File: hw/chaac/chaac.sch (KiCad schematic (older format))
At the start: 94 parts, among them J1 windrain, J10 Solar Panel, J2 RP_SMA, J3 UART, J4 Battery, J5 Power, J6 Light, J7 AM2315, J8 TC2030-CTX, J9 Therm, Q1 Q_PMOS_GSD, SW1 RST, SW2 RST, U1 MIC550X, U2 NRF52811-QFAA, U3 XBEE_S2C, U5 BMP280, U6 MCP73871, Y1 32.768kHz, Y2 32MHz

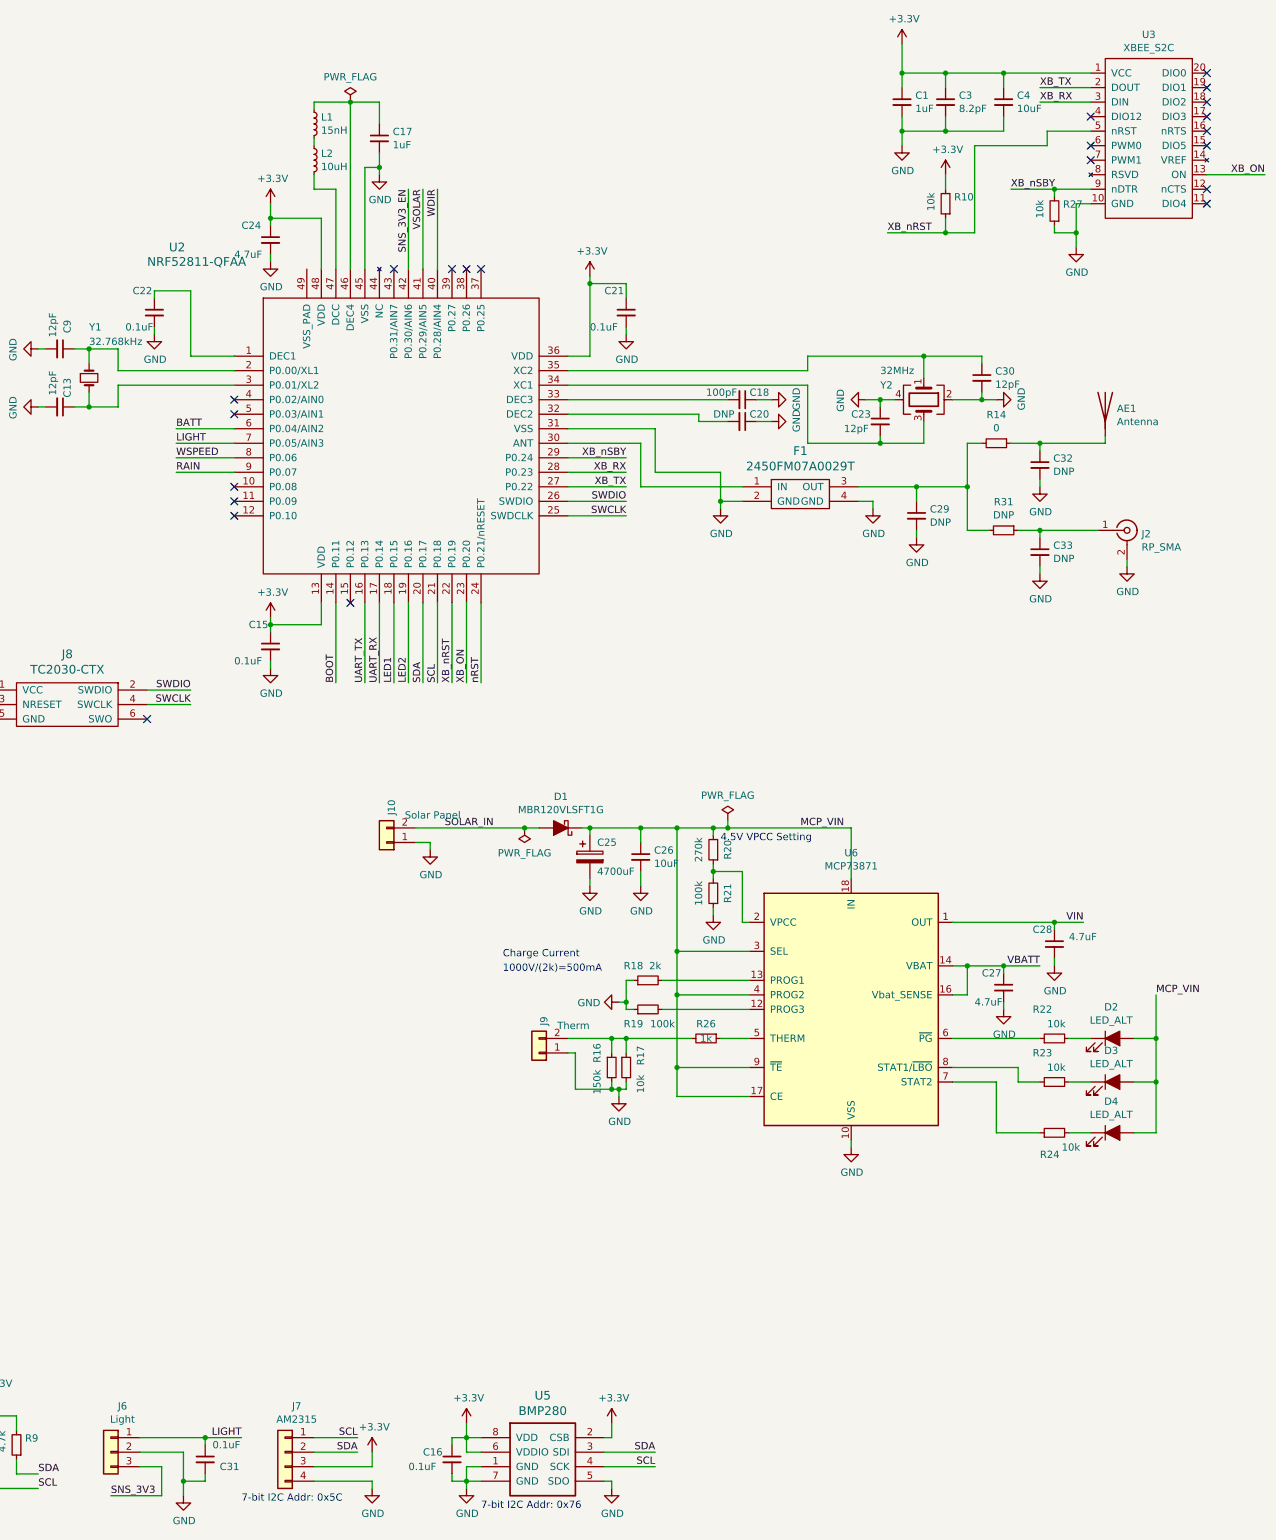
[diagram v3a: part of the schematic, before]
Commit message: Released chaac v2.0 to JLCPCB
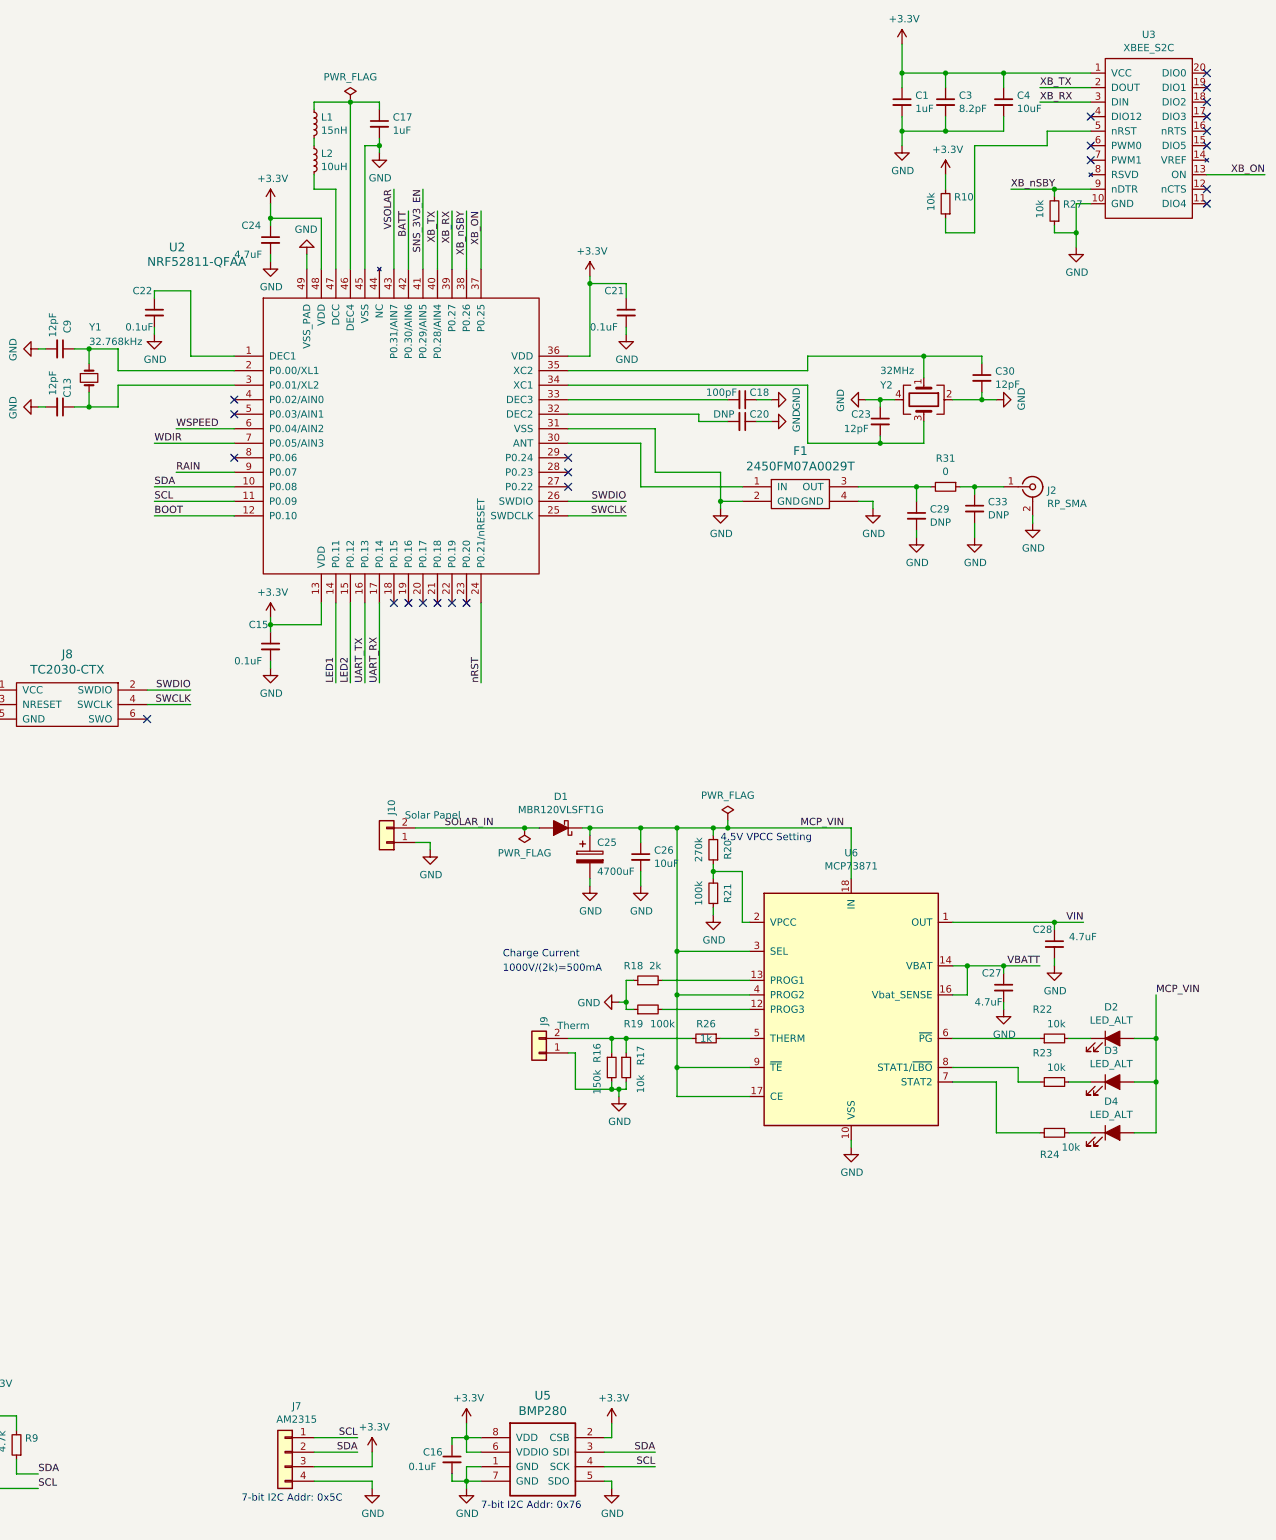
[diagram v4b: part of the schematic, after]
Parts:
- removed AE1: Antenna, alvarop:AMCA31-2R450G-S1F-T3, symbol Device:Antenna
- removed C31: 0.1uF, Capacitor_SMD:C_0603_1608Metric, symbol Device:C_Small
- removed C32: DNP, Capacitor_SMD:C_0402_1005Metric, symbol Device:C_Small
- removed J6: Light, Connector_PinHeader_2.54mm:PinHeader_1x03_P2.54mm_Vertical, symbol Connector_Generic:Conn_01x03
- removed R14: 0, Resistor_SMD:R_0402_1005Metric, symbol Device:R_Small
- C13, C23, C30, C9: DKPN (none) -> 399-1013-1-ND; MPN (none) -> C0402C120J5GACTU
- C15, C21, C22: DKPN (none) -> 490-1318-1-ND; MPN (none) -> GRM155R61A104KA01D
- C17: DKPN (none) -> 311-1438-1-ND; MPN (none) -> CC0402KRX5R5BB105
- C18: DKPN (none) -> 587-1211-1-ND; MPN (none) -> UMK105CG101JV-F
- C20: footprint Capacitor_SMD:C_0603_1608Metric -> Capacitor_SMD:C_0402_1005Metric; DKPN 490-1532-1-ND -> (none); MPN GRM188R71C104KA01D -> (none)
- F1: DKPN (none) -> 712-1623-1-ND; MPN (none) -> 2450FM07A0029T
- J2: DKPN (none) -> SAM8857-ND‎; MPN (none) -> ‎SMA-J-P-H-ST-EM1‎
- L1: DKPN (none) -> 587-1521-1-ND‎; MPN (none) -> HK100515NJ-T‎
- L2: DKPN (none) -> 490-4025-1-ND‎; MPN (none) -> ‎LQM18FN100M00D‎
- R31: value DNP -> 0; DKPN (none) -> 1276-3480-1-ND; MPN (none) -> RC1005J000CS
- U2: footprint alvarop:LQFP48 -> Package_DFN_QFN:QFN-48-1EP_6x6mm_P0.4mm_EP4.6x4.6mm; DKPN (none) -> ‎1490-1075-1-ND‎; MPN (none) -> ‎NRF52811-QFAA-R‎
- Y1: DKPN (none) -> ‎SER4084CT-ND‎; MPN (none) -> FC-135 32.7680KA-AC0
- Y2: DKPN (none) -> 1253-1118-1-ND; MPN (none) -> CX2016DB32000D0FLJCC
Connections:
- net LIGHT is gone; now on net WDIR: U2.7 (P0.05/AIN3)
- net BATT: now also U2.42 (P0.30/AIN6); no longer U2.6 (P0.04/AIN2)
- net BOOT: now also U2.12 (P0.10); no longer U2.14 (P0.11)
- net GND: now also U2.49 (VSS_PAD)
- net LED1: now also U2.14 (P0.11); no longer U2.18 (P0.15)
- net LED2: now also U2.15 (P0.12); no longer U2.19 (P0.16)
- net SCL: now also U2.11 (P0.09); no longer U2.21 (P0.18)
- net SDA: now also U2.10 (P0.08); no longer U2.20 (P0.17)
- net SNS_3V3_EN: now also U2.41 (P0.29/AIN5); no longer U2.42 (P0.30/AIN6)
- net VSOLAR: now also U2.43 (P0.31/AIN7); no longer U2.41 (P0.29/AIN5)
- net WDIR: no longer U2.40 (P0.28/AIN4)
- net WSPEED: now also U2.6 (P0.04/AIN2); no longer U2.8 (P0.06)
- net XB_ON: now also U2.37 (P0.25); no longer U2.23 (P0.20)
- net XB_RX: now also U2.39 (P0.27); no longer U2.28 (P0.23)
- net XB_TX: now also U2.40 (P0.28/AIN4); no longer U2.27 (P0.22)
- net XB_nSBY: now also U2.38 (P0.26); no longer U2.29 (P0.24)
- net XB_nRST: no longer names the net of R10.1, U3.5 (nRST)
- net XB_nRST: no longer U2.22 (P0.19)
- no-connect marks 29 -> 31
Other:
- moved on the sheet: C17, C33, J2, R31

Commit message: Progress with chaac base
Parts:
- removed C1: 1uF, Capacitor_SMD:C_0603_1608Metric, symbol Device:C_Small
- removed C13, C23, C30, C9: 12pF, Capacitor_SMD:C_0402_1005Metric, symbol Device:C_Small
- removed C15, C21, C22: 0.1uF, Capacitor_SMD:C_0402_1005Metric, symbol Device:C_Small
- removed C17: 1uF, Capacitor_SMD:C_0402_1005Metric, symbol Device:C_Small
- removed C18: 100pF, Capacitor_SMD:C_0402_1005Metric, symbol Device:C_Small
- removed C20, C29, C33: DNP, Capacitor_SMD:C_0402_1005Metric, symbol Device:C_Small
- removed C24: 4.7uF, Capacitor_SMD:C_0603_1608Metric, symbol Device:C_Small
- removed C3: 8.2pF, Capacitor_SMD:C_0603_1608Metric, symbol Device:C_Small
- removed C4: 10uF, Capacitor_SMD:C_0603_1608Metric, symbol Device:C_Small
- removed F1: 2450FM07A0029T, alvarop:2450FM07A0029T, symbol alvarop:2450FM07A0029T
- removed J2: RP_SMA, Connector_Coaxial:SMA_Samtec_SMA-J-P-H-ST-EM1_EdgeMount, symbol Connector:Conn_Coaxial
- removed J8: TC2030-CTX, alvarop:TC2030-NL, symbol alvarop:TC2030-CTX
- removed J9: Therm, Connector_PinHeader_2.54mm:PinHeader_1x02_P2.54mm_Vertical, symbol Connector_Generic:Conn_01x02
- removed L1: 15nH, Inductor_SMD:L_0402_1005Metric, symbol Device:L_Small
- removed L2: 10uH, Inductor_SMD:L_0603_1608Metric, symbol Device:L_Small
- removed R10, R27: 10k, Resistor_SMD:R_0603_1608Metric, symbol Device:R_Small
- removed R16: 150k, Resistor_SMD:R_0603_1608Metric, symbol Device:R_Small
- removed R26: 1k, Resistor_SMD:R_0603_1608Metric, symbol Device:R_Small
- removed R31: 0, Resistor_SMD:R_0402_1005Metric, symbol Device:R_Small
- removed U2: NRF52811-QFAA, Package_DFN_QFN:QFN-48-1EP_6x6mm_P0.4mm_EP4.6x4.6mm, symbol alvarop:NRF52811-QFAA
- removed U3: XBEE_S2C, alvarop:XBEE_S2C_TH, symbol alvarop:XBEE_S2C
- removed Y1: 32.768kHz, Crystal:Crystal_SMD_3215-2Pin_3.2x1.5mm, symbol Device:Crystal_Small
- removed Y2: 32MHz, Crystal:Crystal_SMD_2016-4Pin_2.0x1.6mm, symbol Device:Crystal_GND24
- added U2: CHAAC_RADIO, alvarop:CHAAC_RADIO, symbol alvarop:CHAAC_RADIO
- C25: value 4700uF -> 470uF; footprint alvarop:CP_Elec_18x16.5 -> Capacitor_SMD:CP_Elec_8x10; DKPN PCE3461CT-ND -> PCE4178CT-ND; MPN EEV-FK1C472M -> EEE-HA1A471UP
- SW1, SW2: footprint alvarop:PTS645SM43SMTR92 -> alvarop:PTS820J25MSMTRLFS; DKPN CKN9112CT-ND -> CKN10839CT-ND; MPN PTS645SM43SMTR92 LFS -> PTS820J25MSMTRLFS
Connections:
- net labels added: P0.02-AIN0, P0.03-AIN1, P0.04-AIN2, P0.05-AIN3, P0.06, P0.07, P0.08, P0.11, P0.12, P0.13, P0.14, P0.15, P0.16, P0.17, P0.18, P0.19, P0.20, P0.22, P0.23, P0.24, P0.25, P0.26, P0.27, P0.28-AIN4, P0.29-AIN5, P0.30-AIN6, P0.31-AIN7
- net labels removed: SWCLK, SWDIO, XB_ON, XB_RX, XB_TX, XB_nSBY
- wire segments 380 -> 261
- no-connect marks 31 -> 7
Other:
- moved on the sheet: R17

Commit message: Done routing chaac v3.0 base board?
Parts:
- removed C7: DNP, Capacitor_SMD:C_0603_1608Metric, symbol Device:C_Small
- removed J5: Power, Connector_PinHeader_2.54mm:PinHeader_1x03_P2.54mm_Vertical, symbol Connector_Generic:Conn_01x03
- J10: footprint Connector_PinHeader_2.54mm:PinHeader_1x02_P2.54mm_Vertical -> TerminalBlock_TE-Connectivity:TerminalBlock_TE_282834-2_1x02_P2.54mm_Horizontal
- J7: footprint Connector_PinHeader_2.54mm:PinHeader_1x04_P2.54mm_Vertical -> TerminalBlock_TE-Connectivity:TerminalBlock_TE_282834-4_1x04_P2.54mm_Horizontal
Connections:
- net labels removed: P0.02-AIN0, P0.03-AIN1, P0.04-AIN2, P0.05-AIN3, P0.06, P0.07, P0.08, P0.11, P0.12, P0.13, P0.14, P0.15, P0.16, P0.17, P0.18, P0.19, P0.20, P0.22, P0.23, P0.24, P0.25, P0.26, P0.27, P0.28-AIN4, P0.29-AIN5, P0.30-AIN6, P0.31-AIN7
- wire segments 261 -> 243
- no-connect marks 7 -> 23
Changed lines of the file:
@@
 L Connector_Generic:Conn_01x04 J7
 U 1 1 5BAAE247
-P 9050 10450
-F 0 "J7" H 8970 10767 50  0000 C CNN
-F 1 "AM2315" H 8970 10676 50  0000 C CNN
-F 2 "Connector_PinHeader_2.54mm:PinHeader_1x04_P2.54mm_Vertical" H 9050 10450 50  0001 C CNN
-F 3 "~" H 9050 10450 50  0001 C CNN
-F 4 "ED10563-ND" H 0   0   50  0001 C CNN "DKPN"
-F 5 "OSTVN04A150" H 0   0   50  0001 C CNN "MPN"
-	1    9050 10450
-	-1   0    0    -1
+P 9050 10550
+F 0 "J7" H 8970 10867 50  0000 C CNN
+F 1 "AM2315" H 8970 10776 50  0000 C CNN
+F 2 "TerminalBlock_TE-Connectivity:TerminalBlock_TE_282834-4_1x04_P2.54mm_Horizontal" H 9050 10550 50  0001 C CNN
+F 3 "~" H 9050 10550 50  0001 C CNN
+F 4 "ED10563-ND" H 0   100 50  0001 C CNN "DKPN"
+F 5 "OSTVN04A150" H 0   100 50  0001 C CNN "MPN"
+	1    9050 10550
+	-1   0    0    1
 $EndComp
 Wire Wire Line
@@
 Text Label 9550 10350 2    50   ~ 0
 SCL
-$Comp
-L Connector_Generic:Conn_01x03 J5
-U 1 1 5BAB4149
-P 3300 1000
-F 0 "J5" H 3220 1317 50  0000 C CNN
-F 1 "Power" H 3220 1226 50  0000 C CNN
-F 2 "Connector_PinHeader_2.54mm:PinHeader_1x03_P2.54mm_Vertical" H 3300 1000 50  0001 C CNN
-F 3 "~" H 3300 1000 50  0001 C CNN
-	1    3300 1000
-	-1   0    0    -1
-$EndComp
-Wire Wire Line
-	3500 1000 3850 1000
-Wire Wire Line
-	3850 1000 3850 1100
-Wire Wire Line
-	3500 900  3850 900
-Wire Wire Line
-	3850 900  3850 800
-Wire Wire Line
-	3500 1100 3750 1100
-Text Label 3750 1100 2    50   ~ 0
-VIN
-$Comp
-L power:+3.3V #PWR011
-U 1 1 5BAB8AA0
-P 3850 800
-F 0 "#PWR011" H 3850 650 50  0001 C CNN
-F 1 "+3.3V" H 3865 973 50  0000 C CNN
-F 2 "" H 3850 800 50  0001 C CNN
-F 3 "" H 3850 800 50  0001 C CNN
-	1    3850 800
-	1    0    0    -1
-$EndComp
 $Comp
 L power:GND #PWR012
@@
 Text Label 5850 3600 0    50   ~ 0
 nRST
-Wire Wire Line
-	9700 4600 9700 5150
-Wire Wire Line
-	9600 4600 9600 5150
-Text Label 9600 5150 1    50   ~ 0
-UART_TX
-Text Label 9700 5150 1    50   ~ 0
-UART_RX
 $Comp
 L Connector_Generic:Conn_01x03 J3
@@
 BATT
 $Comp
-L power:GND #PWR0133
-U 1 1 5CAFFDD5
-P 3850 1100
-F 0 "#PWR0133" H 3850 850 50  0001 C CNN
-F 1 "GND" H 3855 927 50  0000 C CNN
-F 2 "" H 3850 1100 50  0001 C CNN
-F 3 "" H 3850 1100 50  0001 C CNN
-	1    3850 1100
-	1    0    0    -1
-$EndComp
-$Comp
 L power:GND #PWR0134
 U 1 1 5CAFFF76
@@
 F 0 "J10" V 9716 6062 50  0000 R CNN
 F 1 "Solar Panel" H 9625 6062 50  0000 R CNN
-F 2 "Connector_PinHeader_2.54mm:PinHeader_1x02_P2.54mm_Vertical" H 9750 6250 50  0001 C CNN
+F 2 "TerminalBlock_TE-Connectivity:TerminalBlock_TE_282834-2_1x02_P2.54mm_Horizontal" H 9750 6250 50  0001 C CNN
 F 3 "~" H 9750 6250 50  0001 C CNN
 F 4 "ED10561-ND" H 0   0   50  0001 C CNN "DKPN"
@@
 	2000 4400 2000 4250
 Connection ~ 2000 4250
-$Comp
-L Device:C_Small C7
-U 1 1 5C97805D
-P 2450 4000
-F 0 "C7" H 2250 4050 50  0000 L CNN
-F 1 "DNP" H 2150 3950 50  0000 L CNN
-F 2 "Capacitor_SMD:C_0603_1608Metric" H 2450 4000 50  0001 C CNN
-F 3 "~" H 2450 4000 50  0001 C CNN
-	1    2450 4000
-	1    0    0    -1
-$EndComp
-Wire Wire Line
-	2450 4100 2450 4250
-Wire Wire Line
-	2450 4250 2000 4250
-Wire Wire Line
-	2200 3800 2450 3800
-Wire Wire Line
-	2450 3900 2450 3800
-Connection ~ 2450 3800
 Wire Wire Line
 	2000 4600 2000 4750
 Wire Wire Line
 	2000 4750 1450 4750
-Wire Wire Line
-	2450 3800 2900 3800
 Text Label 1450 4750 0    50   ~ 0
 SNS_3V3_EN
@@
 Wire Wire Line
 	5200 5000 5200 5050
-Text Label 10400 5150 1    50   ~ 0
-nRST
-Wire Wire Line
-	10400 5150 10400 4600
 Wire Wire Line
 	5700 3600 5850 3600
 Connection ~ 5700 3600
-Wire Wire Line
-	9300 4600 9300 4750
 Wire Wire Line
 	2450 3050 2650 3050
@@
 	-1   0    0    1
 $EndComp
-Text Label 9500 5150 1    50   ~ 0
-LED2
-Wire Wire Line
-	9500 4600 9500 5150
-Wire Wire Line
-	9400 4600 9400 5150
-Text Label 9400 5150 1    50   ~ 0
-LED1
-Wire Wire Line
-	11250 2600 11250 2050
-Text Label 11250 2050 3    50   ~ 0
+Wire Wire Line
+	6700 6750 7250 6750
+Text Label 4600 8050 0    50   ~ 0
 SNS_3V3_EN
-Text Label 11150 2200 3    50   ~ 0
-BATT
-Wire Wire Line
-	11150 2600 11150 2200
-Text Label 11050 2050 3    50   ~ 0
-VSOLAR
-Wire Wire Line
-	11050 2600 11050 2050
-Wire Wire Line
-	6700 6750 7250 6750
-Text Label 7250 6750 2    50   ~ 0
-P0.26
 Wire Wire Line
 	6700 6850 7250 6850
-Text Label 7250 6850 2    50   ~ 0
-P0.28-AIN4
 Wire Wire Line
 	6700 6950 7250 6950
-Text Label 7250 6950 2    50   ~ 0
-P0.30-AIN6
 Wire Wire Line
 	6700 7050 7250 7050
-Text Label 7250 7050 2    50   ~ 0
-P0.02-AIN0
 Wire Wire Line
 	6700 7150 7250 7150
 Text Label 7250 7150 2    50   ~ 0
-P0.04-AIN2
+VSOLAR
 Wire Wire Line
 	6700 7250 7250 7250
-Text Label 7250 7250 2    50   ~ 0
-P0.06
 Wire Wire Line
 	6700 7350 7250 7350
-Text Label 7250 7350 2    50   ~ 0
-P0.08
 Wire Wire Line
 	6700 7450 7250 7450
 Wire Wire Line
 	5100 6750 4550 6750
-Text Label 4550 6750 0    50   ~ 0
-P0.25
 Wire Wire Line
 	5100 6850 4550 6850
-Text Label 4550 6850 0    50   ~ 0
-P0.27
 Wire Wire Line
 	5100 6950 4550 6950
-Text Label 4550 6950 0    50   ~ 0
-P0.29-AIN5
 Wire Wire Line
 	5100 7050 4550 7050
-Text Label 4550 7050 0    50   ~ 0
-P0.31-AIN7
 Wire Wire Line
 	5100 7150 4550 7150
-Text Label 4550 7150 0    50   ~ 0
-P0.03-AIN1
 Wire Wire Line
 	5100 7250 4550 7250
 Text Label 4550 7250 0    50   ~ 0
-P0.05-AIN3
+BATT
 Wire Wire Line
 	5100 7350 4550 7350
-Text Label 4550 7350 0    50   ~ 0
-P0.07
-Wire Wire Line
-	5100 7450 4550 7450
+Wire Wire Line
+	7200 8050 6650 8050
 Wire Wire Line
 	5150 8550 4600 8550
+Wire Wire Line
+	5150 8650 4600 8650
 Text Label 4600 8550 0    50   ~ 0
-P0.13
-Wire Wire Line
-	5150 8650 4600 8650
-Text Label 4600 8650 0    50   ~ 0
-P0.11
+WSPEED
 Wire Wire Line
 	5150 8350 4600 8350
-Text Label 4600 8350 0    50   ~ 0
-P0.17
 Wire Wire Line
 	5150 8450 4600 8450
-Text Label 4600 8450 0    50   ~ 0
-P0.15
 Wire Wire Line
 	5150 8150 4600 8150
@@
 Wire Wire Line
 	5150 8250 4600 8250
-Text Label 4600 8250 0    50   ~ 0
-P0.19
 Wire Wire Line
 	5150 7950 4600 7950
 Wire Wire Line
 	5150 8050 4600 8050
-Text Label 4600 8050 0    50   ~ 0
-P0.23
+Wire Wire Line
+	6650 8250 7200 8250
+Text Label 7200 8250 2    50   ~ 0
+SCL
+Text Label 4600 8650 0    50   ~ 0
+RAIN
+Wire Wire Line
+	6650 8450 7200 8450
+Text Label 7200 8450 2    50   ~ 0
+LED1
+Wire Wire Line
+	6650 8150 7200 8150
+Text Label 7200 8150 2    50   ~ 0
+SDA
+Wire Wire Line
+	6650 8650 7200 8650
+Text Label 7200 8650 2    50   ~ 0
+UART_RX
+Wire Wire Line
+	6650 8350 7200 8350
+Text Label 7200 8350 2    50   ~ 0
+LED2
+Wire Wire Line
+	6650 7950 7200 7950
 Wire Wire Line
 	6650 8550 7200 8550
 Text Label 7200 8550 2    50   ~ 0
-P0.14
-Wire Wire Line
-	6650 8650 7200 8650
-Text Label 7200 8650 2    50   ~ 0
-P0.12
-Wire Wire Line
-	6650 8350 7200 8350
-Text Label 7200 8350 2    50   ~ 0
-P0.18
-Wire Wire Line
-	6650 8450 7200 8450
-Text Label 7200 8450 2    50   ~ 0
-P0.16
-Wire Wire Line
-	6650 8150 7200 8150
-Text Label 7200 8150 2    50   ~ 0
-P0.22
-Wire Wire Line
-	6650 8250 7200 8250
-Text Label 7200 8250 2    50   ~ 0
-P0.20
-Wire Wire Line
-	6650 7950 7200 7950
-Wire Wire Line
-	6650 8050 7200 8050
-Text Label 7200 8050 2    50   ~ 0
-P0.24
+UART_TX
 $Comp
 L power:GND #PWR0106
@@
 $Comp
 L alvarop:CHAAC_RADIO U2
-U 1 1 5D1FF521
-P 5100 6750
-F 0 "U2" H 5900 7040 60  0000 C CNN
-F 1 "CHAAC_RADIO" H 5900 6934 60  0000 C CNN
-F 2 "alvarop:CHAAC_RADIO" H 5100 6750 50  0001 C CNN
-F 3 "" H 5100 6750 50  0001 C CNN
-	1    5100 6750
-	1    0    0    -1
-$EndComp
-$Comp
-L alvarop:CHAAC_RADIO U2
 U 2 1 5D2018F9
 P 5150 7950
@@
 	1    0    0    -1
 $EndComp
-Text Label 7250 7450 0    50   ~ 0
-SDA
-Text Label 4550 7450 0    50   ~ 0
-SCL
 Wire Wire Line
 	11350 7900 11350 8000
@@
 	1    0    0    -1
 $EndComp
+Text Label 7250 6850 2    50   ~ 0
+WDIR
+Wire Wire Line
+	2200 3800 2900 3800
+$Comp
+L alvarop:CHAAC_RADIO U2
+U 1 1 5D1FF521
+P 5100 6750
+F 0 "U2" H 5900 7040 60  0000 C CNN
+F 1 "CHAAC_RADIO" H 5900 6934 60  0000 C CNN
+F 2 "alvarop:CHAAC_RADIO" H 5100 6750 50  0001 C CNN
+F 3 "" H 5100 6750 50  0001 C CNN
+	1    5100 6750
+	1    0    0    -1
+$EndComp
+Text Label 7200 8050 2    50   ~ 0
+BOOT
+NoConn ~ 4600 8450
+NoConn ~ 4600 8350
+NoConn ~ 4600 8250
+NoConn ~ 4550 7350
+NoConn ~ 4550 7150
+NoConn ~ 4550 7050
+NoConn ~ 4550 6950
+NoConn ~ 4550 6850
+NoConn ~ 4550 6750
+NoConn ~ 7250 6750
+NoConn ~ 7250 6950
+NoConn ~ 7250 7250
+NoConn ~ 7250 7350
+NoConn ~ 7250 7450
+NoConn ~ 7250 7050
+Wire Wire Line
+	5100 7450 4550 7450
+NoConn ~ 4550 7450
 $EndSCHEMATC

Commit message: re-annotated schematic/board
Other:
- moved on the sheet: C10, C11, C12, C14, C16, C19, C2, C25, C26, C27, C28, C5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
